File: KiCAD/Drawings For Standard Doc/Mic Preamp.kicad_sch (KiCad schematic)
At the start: 13 parts, among them Q1 S9013

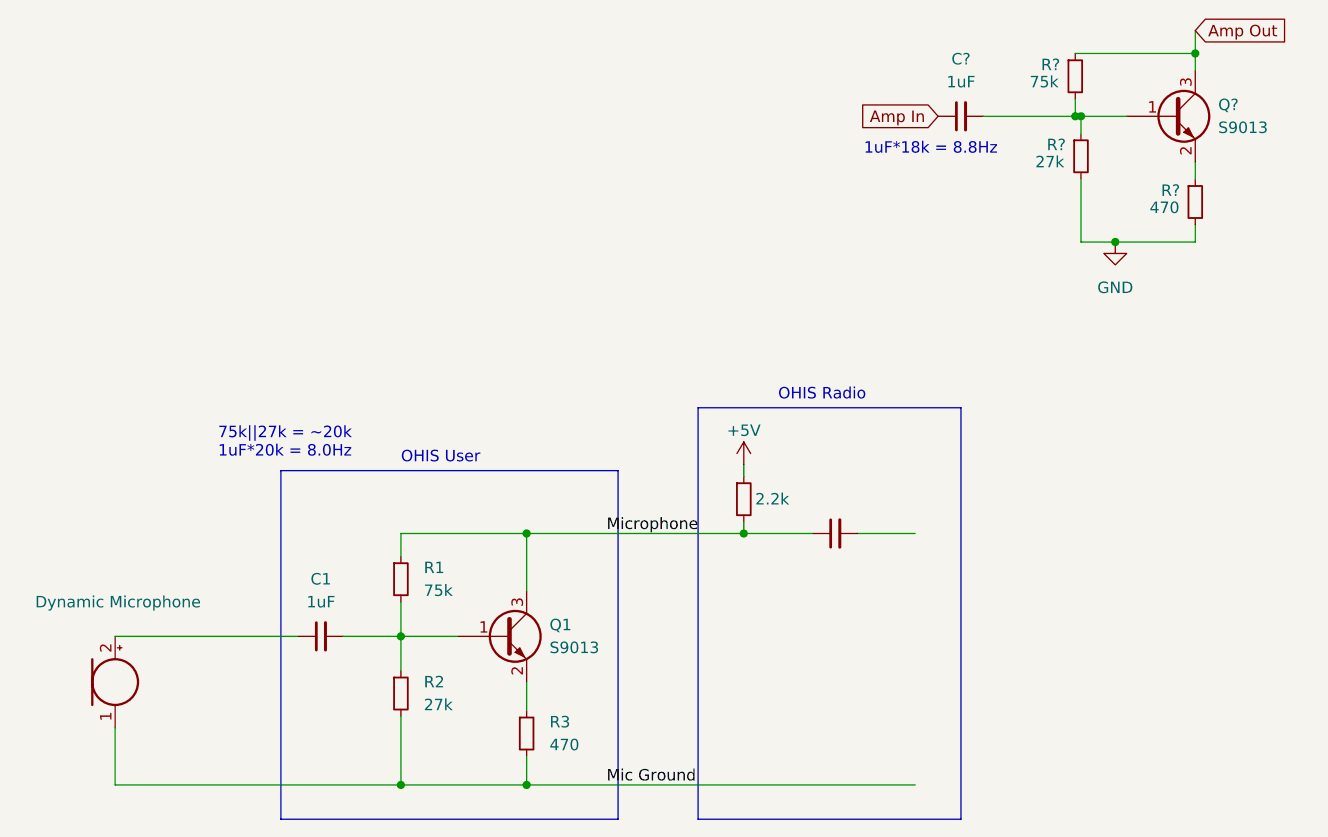
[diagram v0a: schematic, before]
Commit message: Creating generic slide show. Added Overview diagram.
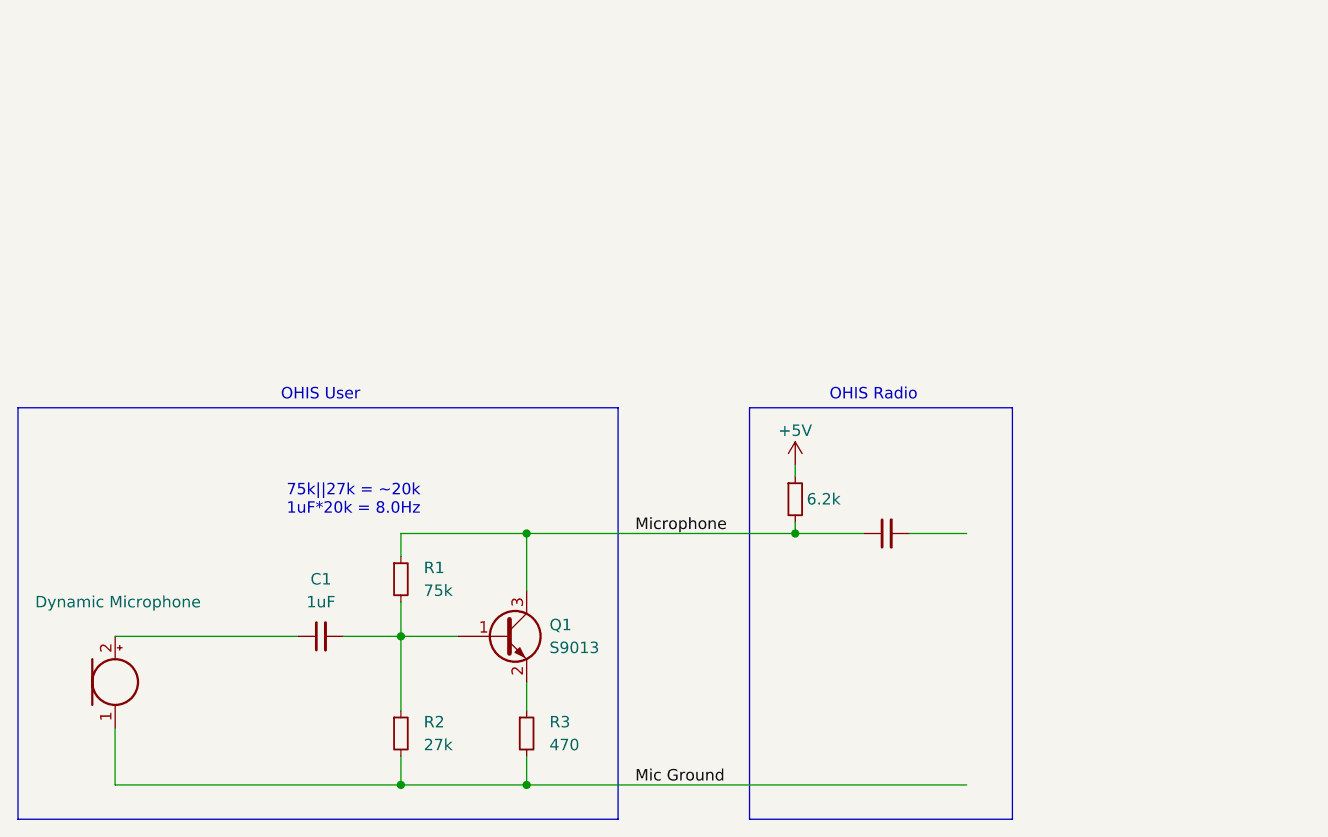
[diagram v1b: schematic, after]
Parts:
- removed C?: 1uF, Capacitor_SMD:C_0603_1608Metric_Pad1.08x0.95mm_HandSolder, symbol Device:C_Small
- removed Q?: S9013, Package_TO_SOT_SMD:SOT-23, symbol Transistor_BJT:MMBT3904
- removed R?: 75k, Resistor_SMD:R_0603_1608Metric_Pad0.98x0.95mm_HandSolder, symbol Device:R_Small
- removed R?: 27k, Resistor_SMD:R_0603_1608Metric_Pad0.98x0.95mm_HandSolder, symbol Device:R_Small
- removed R?: 470, Resistor_SMD:R_0603_1608Metric_Pad0.98x0.95mm_HandSolder, symbol Device:R_Small
- R?: value 2.2k -> 6.2k
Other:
- note removed: "1uF*18k = 8.8Hz"
- moved on the sheet: R2
